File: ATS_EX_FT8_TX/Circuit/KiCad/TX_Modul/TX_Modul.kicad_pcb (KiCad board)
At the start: 2 copper layers, 73 x 50 mm, 21 parts, among them J1 Conn_01x15_Socket, J2 Conn_01x15_Socket, J3 From PC, J4 Relais, J6 Conn_01x06_Socket, J7 Conn_01x06_Socket, J8 Conn_01x06_Socket

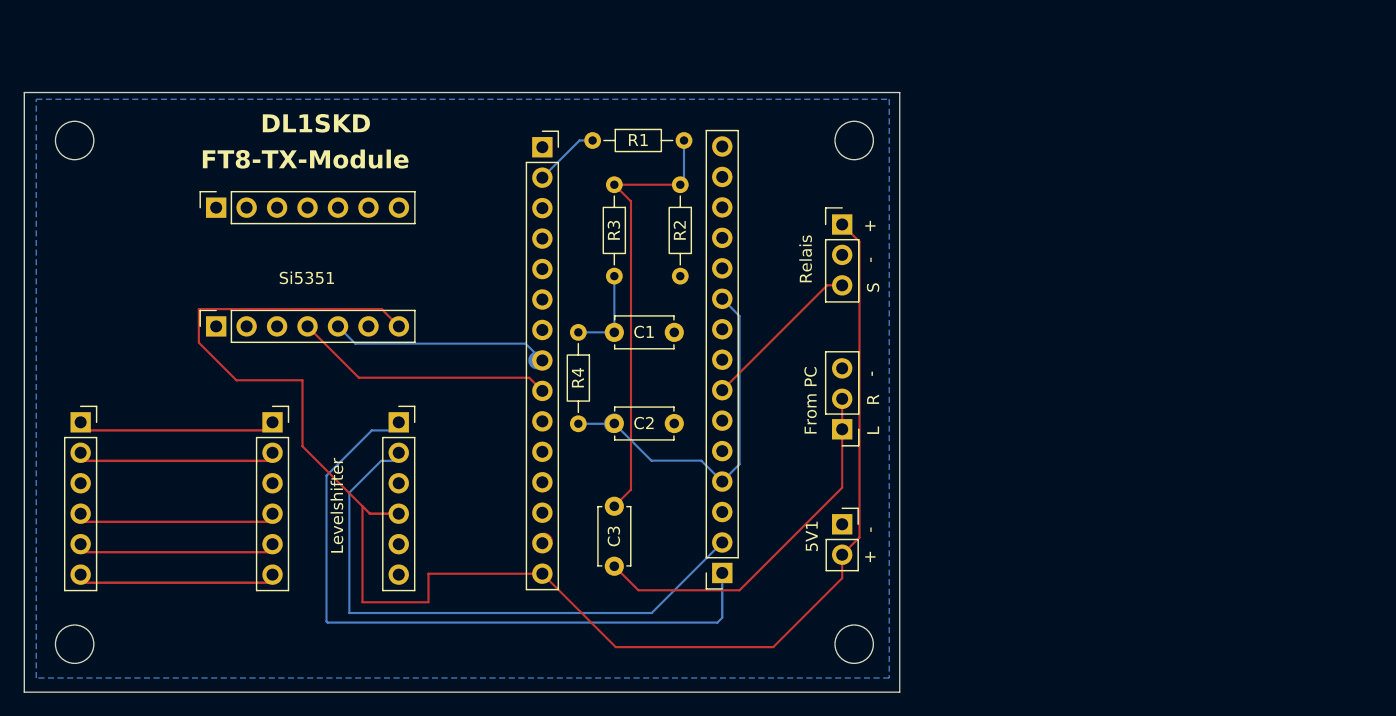
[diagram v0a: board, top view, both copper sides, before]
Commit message: LEDs added
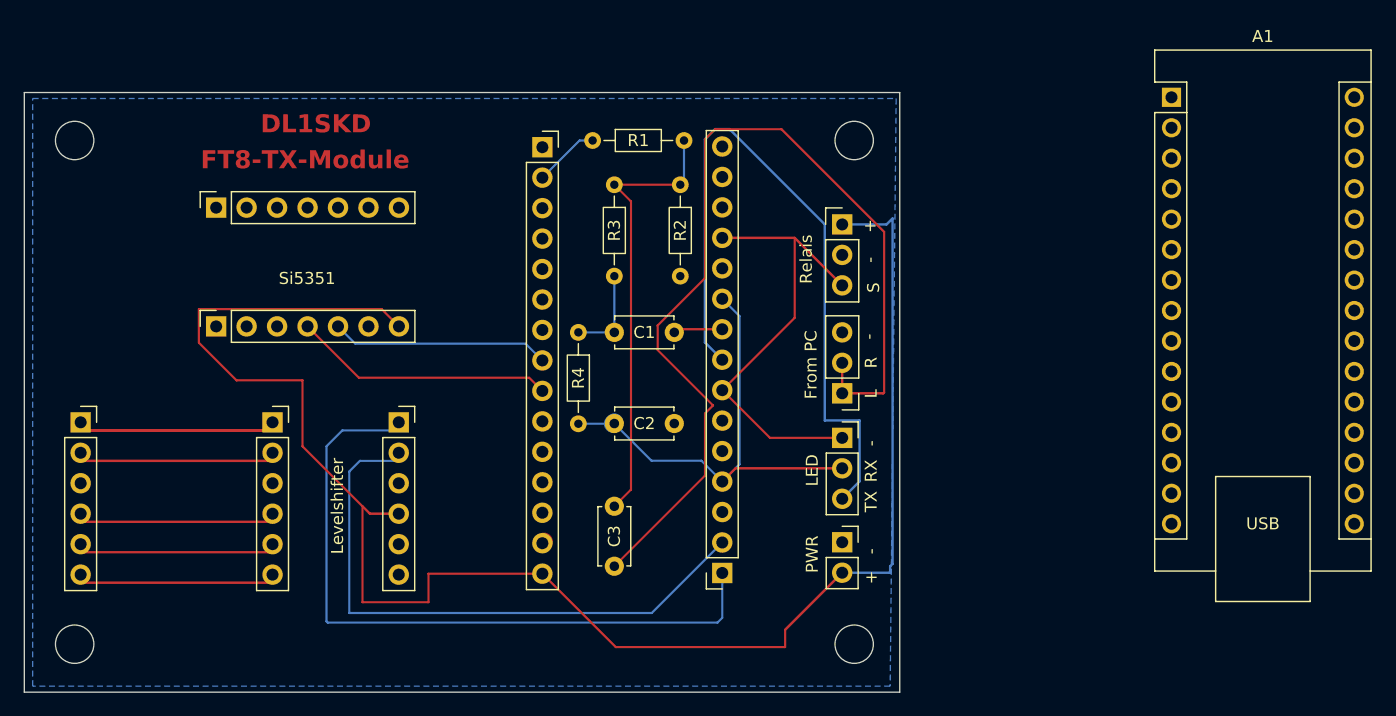
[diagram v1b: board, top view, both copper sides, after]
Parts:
- added A1: Arduino_Nano_v3.x, Module:Arduino_Nano, F.Cu at (209.0, 35.4)
- added J9: StatusLED, Connector_PinSocket_2.54mm:PinSocket_1x03_P2.54mm_Vertical, F.Cu at (181.5, 63.8)
- moved J3 3.00 mm to (181.5, 60.1)
- moved 5V1 1.50 mm to (181.5, 72.5)
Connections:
- J2 pad 12: unconnected-(J2-Pin_12-Pad12) -> Net-(J2-Pin_12)
- J2 pad 7: Net-(J2-Pin_7) -> Net-(J2-Pin_12)
- J2 pad 8: unconnected-(J2-Pin_8-Pad8) -> Net-(J2-Pin_8)
- J4 pad 3: Net-(J2-Pin_7) -> Net-(J2-Pin_12)
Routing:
- net Net-(J2-Pin_8): track 0.00 -> 59.0 mm
- net Net-(C3-+): track 30.8 -> 80.8 mm
- net Net-(J2-Pin_12): track 0.00 -> 37.8 mm
- net Net-(J6-Pin_1): track 16.0 -> 32.0 mm
- net Net-(J2-Pin_7): track 13.6 -> 0.00 mm
- net Net-(C2-+): track 30.6 -> 41.1 mm
- net Net-(J1-Pin_15): track 131.9 -> 140.2 mm
- net GND: track 0.89 -> 5.00 mm
- net Net-(J2-Pin_1): track 56.7 -> 58.1 mm
- net Net-(J2-Pin_2): track 48.8 -> 49.8 mm
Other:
- board text added: "LED"
- board text added: "PWR"
- board text added: "RX"
- board text added: "TX"

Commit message: Gerber changed
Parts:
- removed A1: Arduino_Nano_v3.x, Module:Arduino_Nano
